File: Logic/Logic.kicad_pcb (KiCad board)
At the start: 2 copper layers, 11 x 42 mm, 16 parts, among them J1 Conn_01x04_Pin

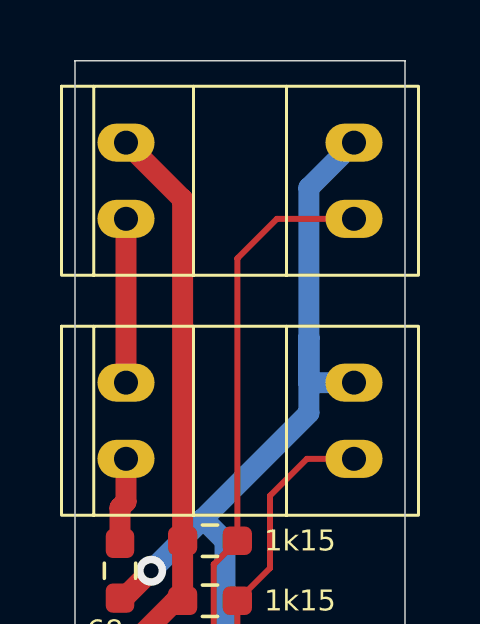
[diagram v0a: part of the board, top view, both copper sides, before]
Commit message: RC2
add fab s/n placeholder
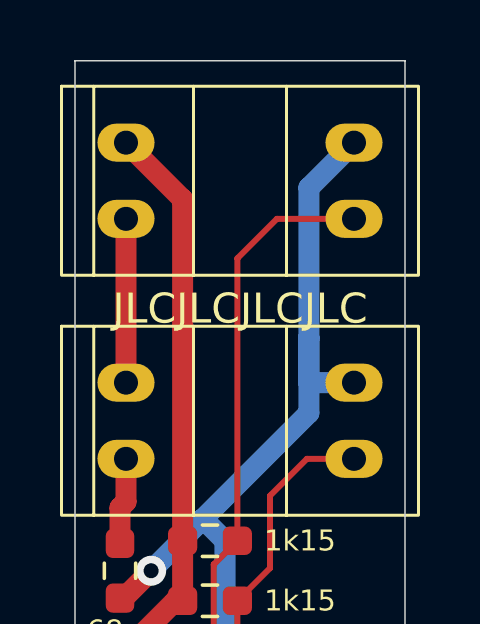
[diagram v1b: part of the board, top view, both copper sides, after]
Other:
- board text added: "JLCJLCJLCJLC"
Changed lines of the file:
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@@
 		(layer "Edge.Cuts")
+	)
+	(gr_text "JLCJLCJLCJLC"
+		(at 148.5 80.85 0)
+		(layer "F.SilkS")
+		(effects
+			(font
+				(size 1 1)
+				(thickness 0.1)
+			)
+			(justify bottom)
+		)
 	)
 	(dimension
